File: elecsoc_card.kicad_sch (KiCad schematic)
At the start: 33 parts, among them J1 Conn_01x02_Pin, J2 Conn_01x02_Pin, U1 NA555D

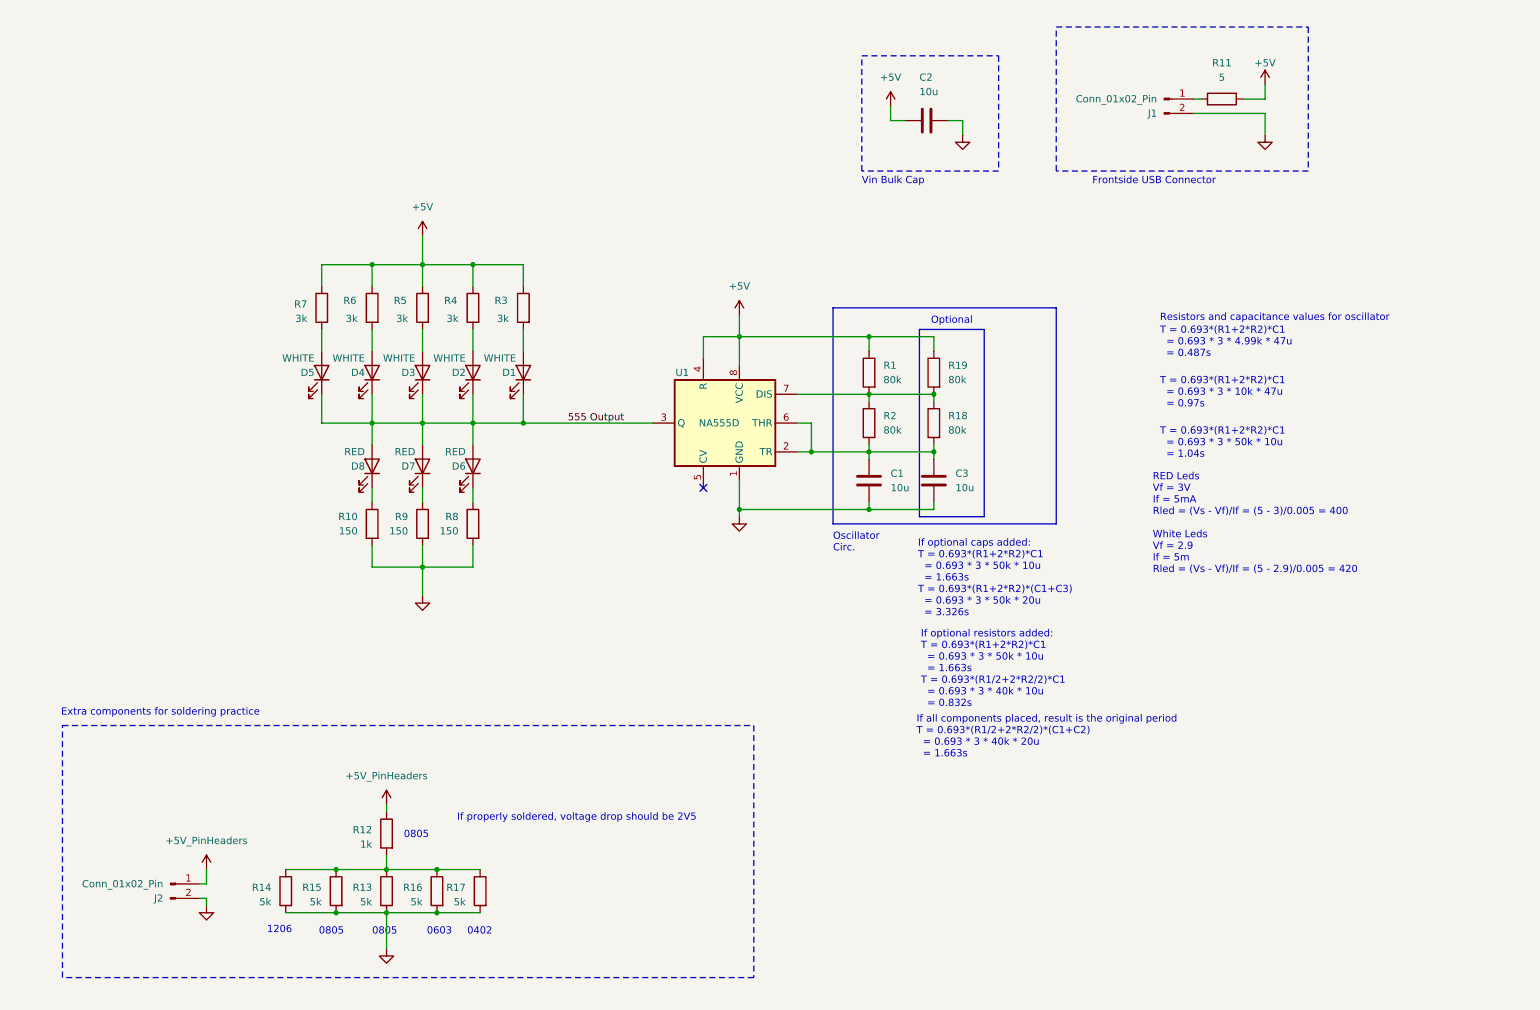
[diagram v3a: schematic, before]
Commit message: updated footprints, consolidated bom
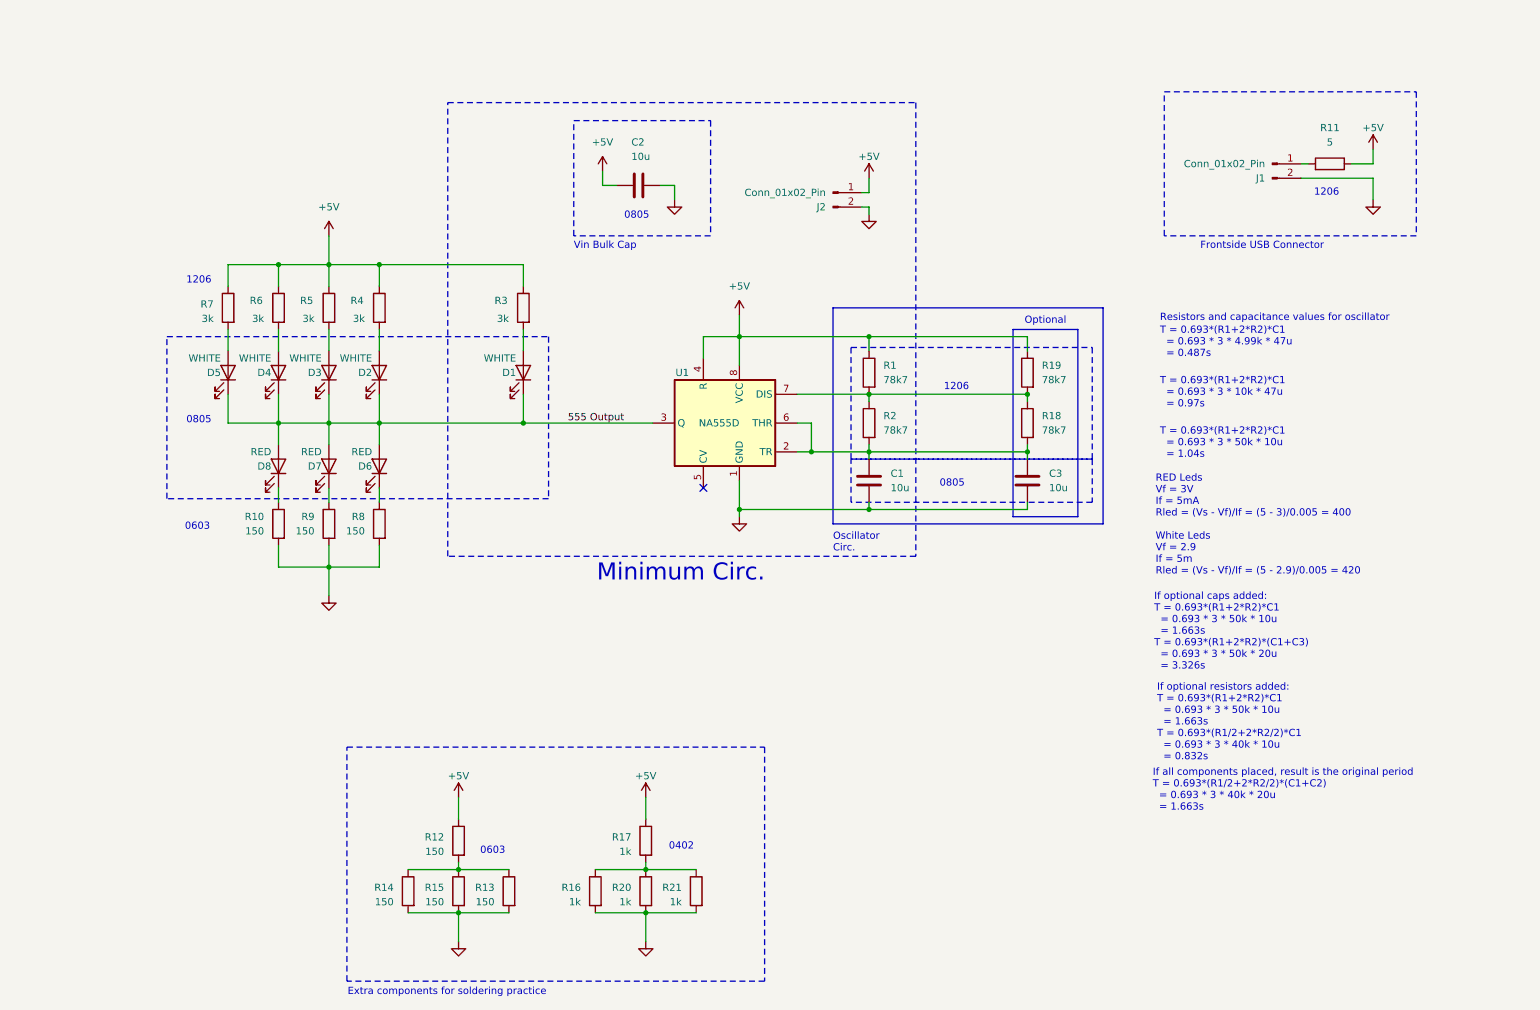
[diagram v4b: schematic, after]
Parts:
- added R20, R21: 1k, Resistor_SMD:R_0805_2012Metric_Pad1.20x1.40mm_HandSolder, symbol Device:R
- R1, R18, R19, R2: value 80k -> 78k7
- R12: value 1k -> 150
- R13, R14, R15: value 5k -> 150
- R16: value 5k -> 1k; footprint Resistor_SMD:R_0603_1608Metric -> Resistor_SMD:R_1206_3216Metric
- R17: value 5k -> 1k; footprint Resistor_SMD:R_0402_1005Metric -> Resistor_SMD:R_0805_2012Metric_Pad1.20x1.40mm_HandSolder
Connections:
- net +5V_PinHeaders is gone; now on net +5V: J2.1 (Pin_1), R12.1
- net +5V: now also R17.1
- net GND: now also R20.2, R21.2; no longer R17.2
- net at R12.2, R13.1, R14.1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: no longer R16.1, R17.1
- new net: R16.1, R17.2, R20.1, R21.1
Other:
- note added: "Minimum Circ."
- note removed: "If properly soldered, voltage drop should be 2V5"
- moved on the sheet: C2, C3, D2, D3, D4, D5, D6, D7, D8, J1, J2, R10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

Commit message: Package sizes updated
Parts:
- R1, R11, R18, R19, R2, R3, R4, R5, R6, R7: footprint Resistor_SMD:R_0805_2012Metric_Pad1.20x1.40mm_HandSolder -> Resistor_SMD:R_1206_3216Metric
- R10, R12, R13, R15, R8, R9: footprint Resistor_SMD:R_0805_2012Metric_Pad1.20x1.40mm_HandSolder -> Resistor_SMD:R_0603_1608Metric
- R14: footprint Resistor_SMD:R_1206_3216Metric -> Resistor_SMD:R_0603_1608Metric
- R16: footprint Resistor_SMD:R_1206_3216Metric -> Resistor_SMD:R_0402_1005Metric
- R17, R20, R21: footprint Resistor_SMD:R_0805_2012Metric_Pad1.20x1.40mm_HandSolder -> Resistor_SMD:R_0402_1005Metric
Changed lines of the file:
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@@
 			)
 		)
-		(property "Footprint" "Resistor_SMD:R_0805_2012Metric_Pad1.20x1.40mm_HandSolder"
+		(property "Footprint" "Resistor_SMD:R_1206_3216Metric"
 			(at 122.428 71.12 90)
 			(effects
@@
 			)
 		)
-		(property "Footprint" "Resistor_SMD:R_0805_2012Metric_Pad1.20x1.40mm_HandSolder"
+		(property "Footprint" "Resistor_SMD:R_1206_3216Metric"
 			(at 211.328 82.55 90)
 			(effects
@@
 			)
 		)
-		(property "Footprint" "Resistor_SMD:R_0805_2012Metric_Pad1.20x1.40mm_HandSolder"
+		(property "Footprint" "Resistor_SMD:R_1206_3216Metric"
 			(at 88.138 71.12 90)
 			(effects
@@
 		(exclude_from_sim no)
 		(in_bom yes)
-		(on_board yes)
+		(on_board no)
 		(dnp no)
 		(property "Reference" "R16"
@@
 			)
 		)
-		(property "Footprint" "Resistor_SMD:R_1206_3216Metric"
+		(property "Footprint" "Resistor_SMD:R_0402_1005Metric"
 			(at 135.128 173.99 90)
 			(effects
@@
 			)
 		)
-		(property "Footprint" "Resistor_SMD:R_1206_3216Metric"
+		(property "Footprint" "Resistor_SMD:R_0603_1608Metric"
 			(at 102.108 173.99 90)
 			(effects
@@
 			)
 		)
-		(property "Footprint" "Resistor_SMD:R_0805_2012Metric_Pad1.20x1.40mm_HandSolder"
+		(property "Footprint" "Resistor_SMD:R_0402_1005Metric"
 			(at 144.018 165.1 90)
 			(effects
@@
 			)
 		)
-		(property "Footprint" "Resistor_SMD:R_0805_2012Metric_Pad1.20x1.40mm_HandSolder"
+		(property "Footprint" "Resistor_SMD:R_1206_3216Metric"
 			(at 262.89 47.498 90)
 			(effects
@@
 			)
 		)
-		(property "Footprint" "Resistor_SMD:R_0805_2012Metric_Pad1.20x1.40mm_HandSolder"
+		(property "Footprint" "Resistor_SMD:R_0402_1005Metric"
 			(at 152.908 173.99 90)
 			(effects
@@
 			)
 		)
-		(property "Footprint" "Resistor_SMD:R_0805_2012Metric_Pad1.20x1.40mm_HandSolder"
+		(property "Footprint" "Resistor_SMD:R_0603_1608Metric"
 			(at 110.998 165.1 90)
 			(effects
@@
 			)
 		)
-		(property "Footprint" "Resistor_SMD:R_0805_2012Metric_Pad1.20x1.40mm_HandSolder"
+		(property "Footprint" "Resistor_SMD:R_1206_3216Metric"
 			(at 79.248 71.12 90)
 			(effects
@@
 			)
 		)
-		(property "Footprint" "Resistor_SMD:R_0805_2012Metric_Pad1.20x1.40mm_HandSolder"
+		(property "Footprint" "Resistor_SMD:R_0603_1608Metric"
 			(at 88.138 109.22 90)
 			(effects
@@
 			)
 		)
-		(property "Footprint" "Resistor_SMD:R_0805_2012Metric_Pad1.20x1.40mm_HandSolder"
+		(property "Footprint" "Resistor_SMD:R_0603_1608Metric"
 			(at 119.888 173.99 90)
 			(effects
@@
 			)
 		)
-		(property "Footprint" "Resistor_SMD:R_0805_2012Metric_Pad1.20x1.40mm_HandSolder"
+		(property "Footprint" "Resistor_SMD:R_0603_1608Metric"
 			(at 97.028 109.22 90)
 			(effects
@@
 			)
 		)
-		(property "Footprint" "Resistor_SMD:R_0805_2012Metric_Pad1.20x1.40mm_HandSolder"
+		(property "Footprint" "Resistor_SMD:R_0603_1608Metric"
 			(at 79.248 109.22 90)
 			(effects
@@
 			)
 		)
-		(property "Footprint" "Resistor_SMD:R_0805_2012Metric_Pad1.20x1.40mm_HandSolder"
+		(property "Footprint" "Resistor_SMD:R_0603_1608Metric"
 			(at 110.998 173.99 90)
 			(effects
@@
 			)
 		)
-		(property "Footprint" "Resistor_SMD:R_0805_2012Metric_Pad1.20x1.40mm_HandSolder"
+		(property "Footprint" "Resistor_SMD:R_1206_3216Metric"
 			(at 70.358 71.12 90)
 			(effects
@@
 			)
 		)
-		(property "Footprint" "Resistor_SMD:R_0805_2012Metric_Pad1.20x1.40mm_HandSolder"
+		(property "Footprint" "Resistor_SMD:R_1206_3216Metric"
 			(at 183.388 91.44 90)
 			(effects
@@
 			)
 		)
-		(property "Footprint" "Resistor_SMD:R_0805_2012Metric_Pad1.20x1.40mm_HandSolder"
+		(property "Footprint" "Resistor_SMD:R_1206_3216Metric"
 			(at 97.028 71.12 90)
 			(effects
@@
 			)
 		)
-		(property "Footprint" "Resistor_SMD:R_0805_2012Metric_Pad1.20x1.40mm_HandSolder"
+		(property "Footprint" "Resistor_SMD:R_1206_3216Metric"
 			(at 183.388 82.55 90)
 			(effects
@@
 			)
 		)
-		(property "Footprint" "Resistor_SMD:R_0805_2012Metric_Pad1.20x1.40mm_HandSolder"
+		(property "Footprint" "Resistor_SMD:R_0402_1005Metric"
 			(at 144.018 173.99 90)
 			(effects
@@
 			)
 		)
-		(property "Footprint" "Resistor_SMD:R_0805_2012Metric_Pad1.20x1.40mm_HandSolder"
+		(property "Footprint" "Resistor_SMD:R_1206_3216Metric"
 			(at 211.328 91.44 90)
 			(effects

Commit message: PCB finished plus gerbers
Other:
- note added: "ElecSoc Soldering Practice Card"
- note added: "Pin Headers"
- moved on the sheet: C1, C2, C3, D1, D2, D3, D4, D5, D6, D7, D8, J1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

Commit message: BOM generated
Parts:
- C1, C2, C3: MPN (none) -> CL21A106KPFNNNF
- D1, D2, D3, D5: MPN (none) -> SMLMN2WB1CW1; Mfr. No. SMLMN2WB1CW1 -> (none)
- D4: MPN (none) -> SMLMN2WB1CW1; Mfr. No SMLMN2WB1CW1 -> (none)
- D6, D7: MPN (none) -> IN-S85AT5UW; Mfr. No. IN-S85AT5UW -> (none)
- D8: MPN (none) -> IN-S85AT5UW; Mfr. No: IN-S85AT5UW -> (none)
- J1: now left out of the parts list
- J2: MPN (none) -> 826632-1
- R1, R18, R19, R2: MPN (none) -> RT1206FRE0778K7L
- R10, R12, R13, R14, R15, R8, R9: MPN (none) -> MCT06030C1500FP500
- R11: MPN (none) -> RT1206FRD075R1L
- R16, R17, R20, R21: MPN (none) -> MCS04020C1001FE000
- R3, R4, R5, R6, R7: MPN (none) -> RT1206FRE073KL
- U1: MPN (none) -> 621-NE555S-13; Mfr. No: 621-NE555S-13 -> (none)
